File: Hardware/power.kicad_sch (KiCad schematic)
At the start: 31 parts, among them U10 RT9080-3.3, U5 LM66200, U6 AP63357DV-7, U7 LM66200, U8 MAX17048, U9 MCP73831

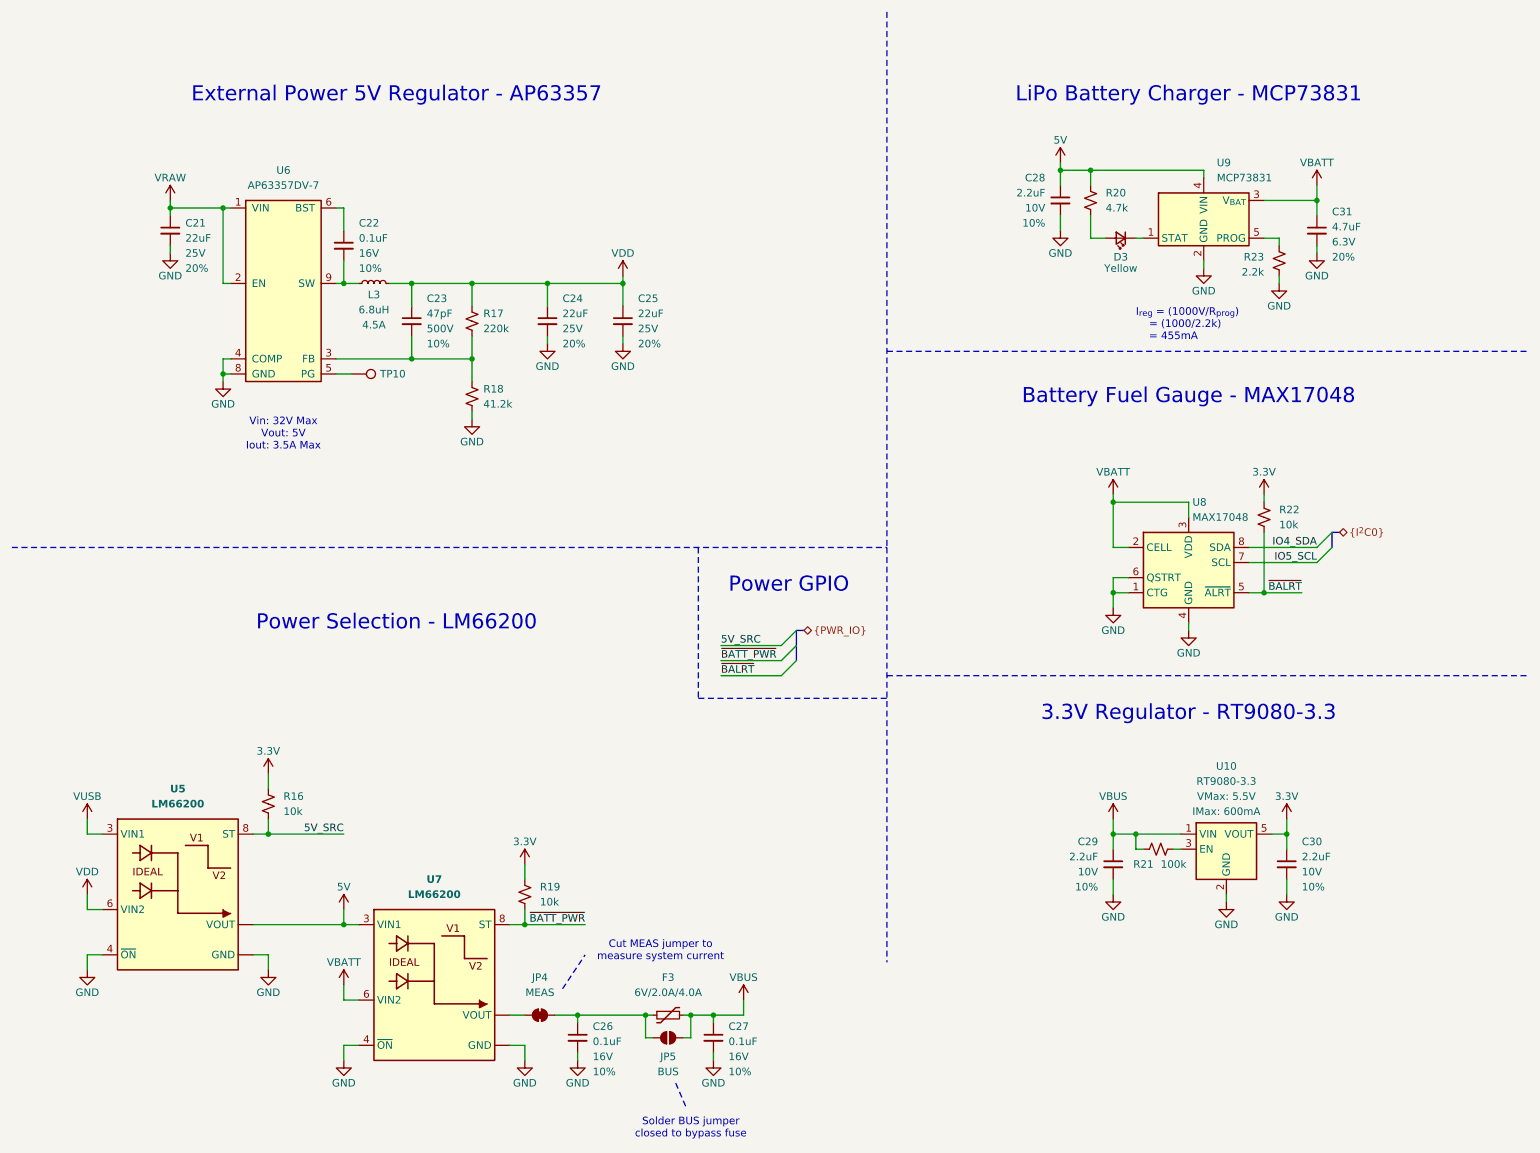
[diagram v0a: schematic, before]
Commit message: Update v01 from checklist. Added measures.
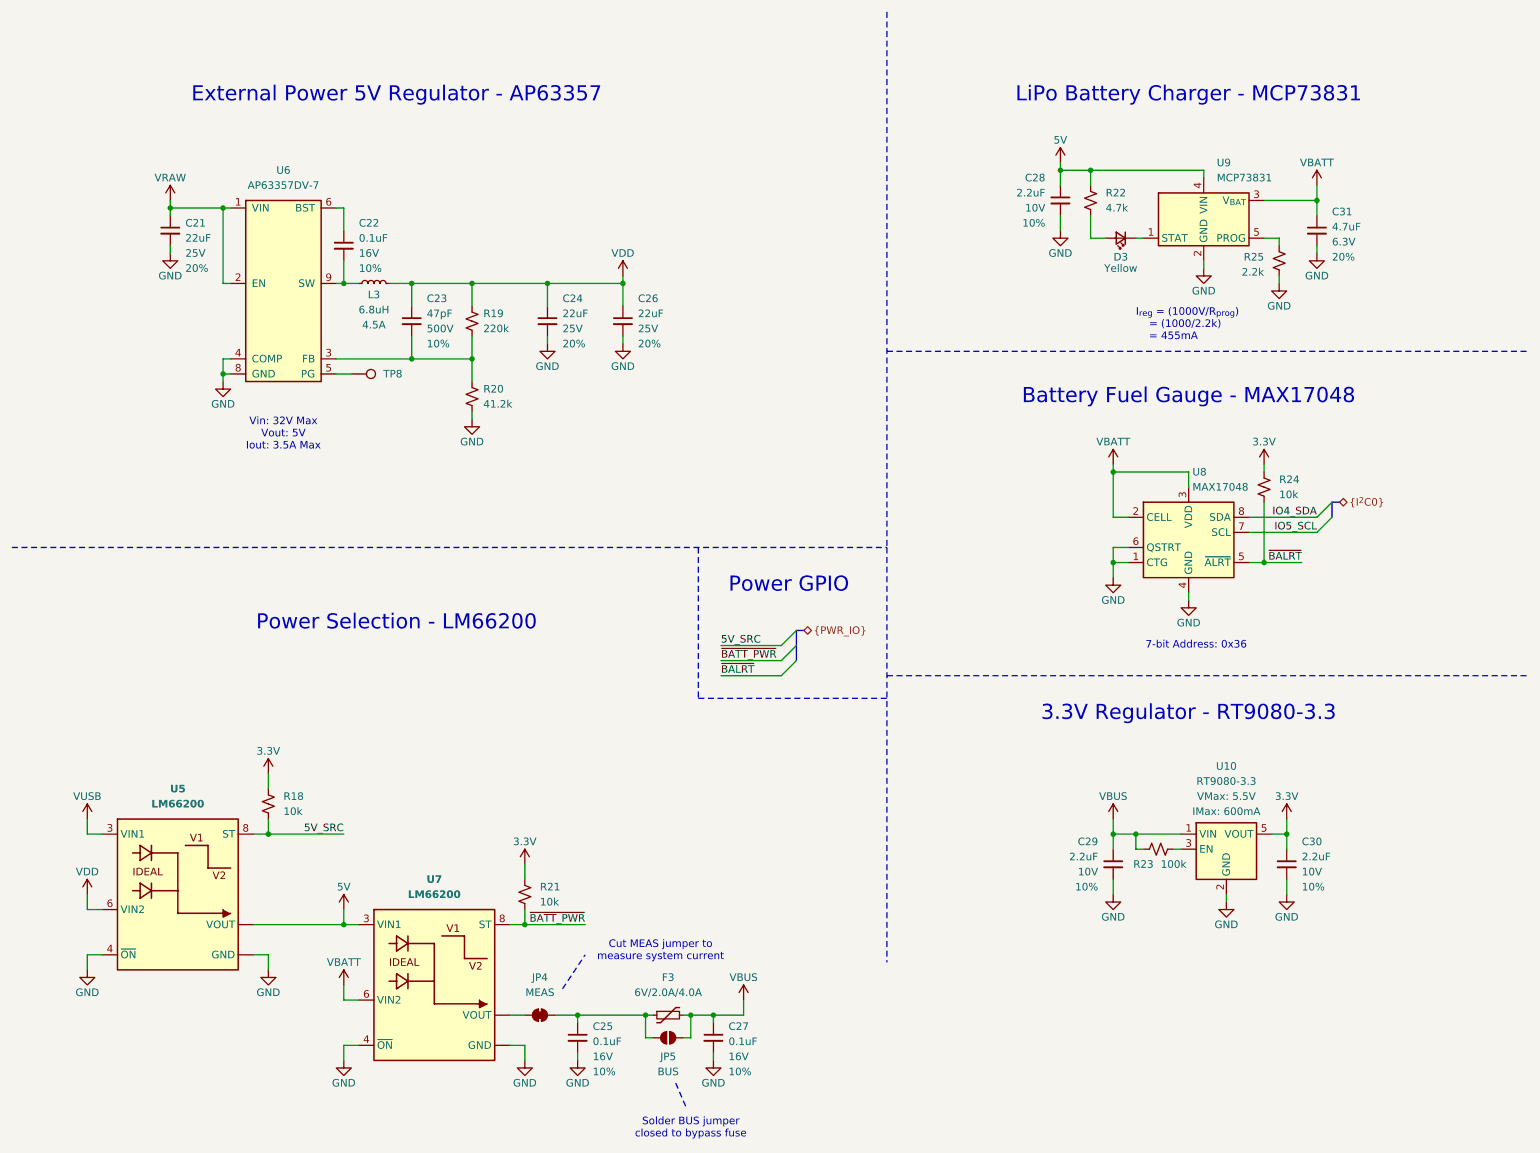
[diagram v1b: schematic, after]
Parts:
- renumbered C26 to C25, C25 to C26, R16 to R18, R17 to R19, R18 to R20, R19 to R21, R20 to R22, R21 to R23, R22 to R24, R23 to R25, TP10 to TP8
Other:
- note added: "7-bit Address: 0x36"
- moved on the sheet: R24, U8

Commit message: v01 post design review changes. Panelize/CAM.
Remove F3.
Added switched power for qwiic, rgb, sd.
Update USB diode for prod friendly package.
Added debounce cap on User button.
Swap user and boot buttons.
Make F2 a smaller package.
Renumber GPIO and use contiguous numbers for PIO purposes.
Swap inputs on Ideal diodes for battery powered current purposes.
Move USB termination resistors closer to MCU.
Fixed A0-A5 ordering.
Update silks.
Add mask to middle of SMD GPIOs.
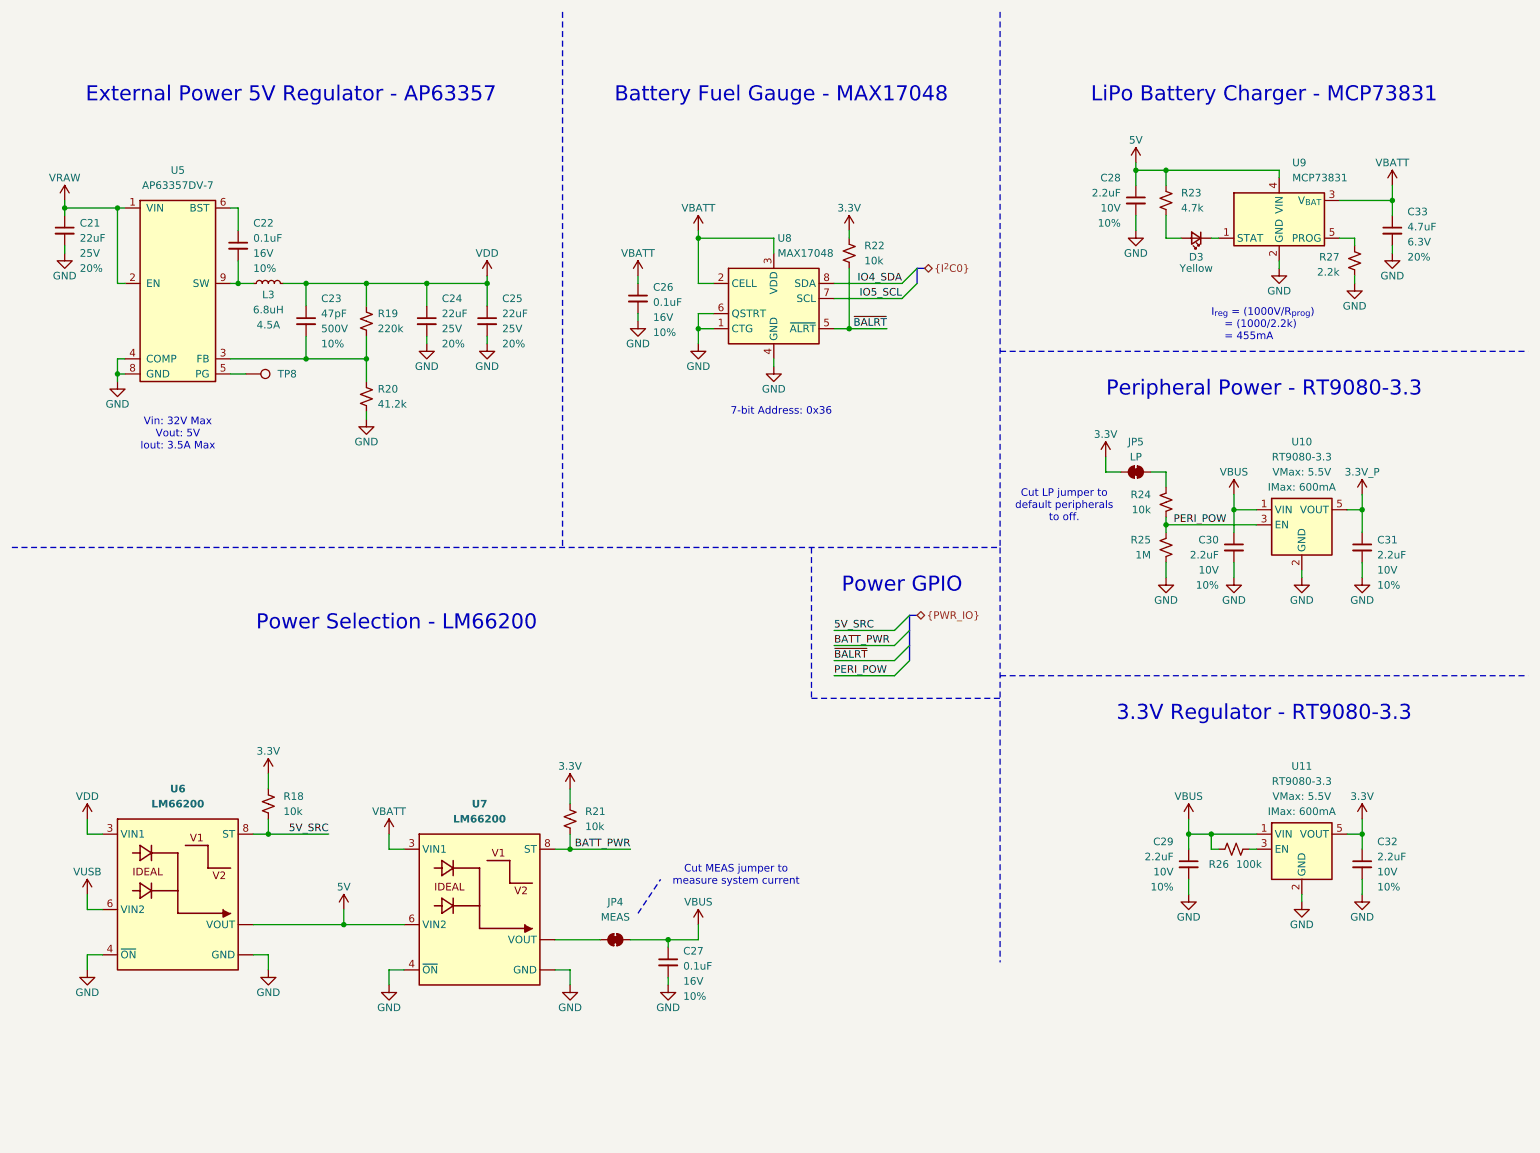
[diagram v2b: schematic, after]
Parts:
- removed C25: 0.1uF, SparkFun-Capacitor:C_0402_1005Metric, symbol SparkFun-Capacitor:0.1uF_0402_16V_10%
- removed F3: 6V/2.0A/4.0A, SparkFun-Fuse:1210, symbol SparkFun-Fuse:Fuse 6V/2.0A/4.0A
- removed JP5: BUS, SparkFun-Jumper:Jumper_2_NO, symbol SparkFun-Jumper:SolderJumper_2_Open
- added C26: 0.1uF, SparkFun-Capacitor:C_0402_1005Metric, symbol SparkFun-Capacitor:0.1uF_0402_16V_10%
- added C30, C31: 2.2uF, SparkFun-Capacitor:C_0402_1005Metric, symbol SparkFun-Capacitor:2.2uF_0402_10V_10%
- added JP5: LP, SparkFun-Jumper:Jumper_2_NC_Trace, symbol SparkFun-Jumper:SolderJumper_2_Bridged
- added R24: 10k, SparkFun-Resistor:R_0402_1005Metric, symbol SparkFun-Resistor:10k_0402
- added R25: 1M, SparkFun-Resistor:R_0402_1005Metric, symbol SparkFun-Resistor:1M_0402
- added U10: RT9080-3.3, SparkFun-Semiconductor-Standard:SOT23-5, symbol SparkFun-Regulator:RT9080-3.3
- renumbered C26 to C25, C30 to C32, C31 to C33, R24 to R22, R22 to R23, R23 to R26, R25 to R27, U10 to U11, U6 to U5, U5 to U6
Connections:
- net 3.3V: now also JP5.1 (A)
- net 5V: now also U7.6 (VIN2); no longer U7.3 (VIN1)
- net GND: now also C26.2, C30.2, C31.2, R25.1, U10.2 (GND)
- net VBATT: now also U7.3 (VIN1), C26.1; no longer U7.6 (VIN2)
- net VBUS: now also JP4.2 (B), C30.1, U10.1 (VIN)
- net VDD: now also U6.3 (VIN1); no longer U6.6 (VIN2)
- net VUSB: now also U6.6 (VIN2); no longer U6.3 (VIN1)
- net ~{BATT_PWR} renamed BATT_PWR
- new net: JP5.2 (B), R24.1
- new net 3.3V_P: C31.1, U10.5 (VOUT)
- new net PERI_POW: R24.2, R25.2, U10.3 (EN)
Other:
- note added: "Cut LP jumper to default peripherals to off."
- note added: "Peripheral Power - RT9080-3.3"
- note removed: "Solder BUS jumper closed to bypass fuse"
- moved on the sheet: C21, C22, C23, C24, C25, C27, C28, C29, C32, C33, D3, JP4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

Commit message: Update for reds
Change version number to v10.
Make user button number correct.
Rotate HSTX conn 180 degrees electrically.
Add silk for HSTX contact direction.
Increase silk text size where it made sense.
Increase silk label length on PTHs.
Panelize and CAM.
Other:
- title: Power Generation and Battery Management -> Power and Battery Management
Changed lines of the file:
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@@
 	(paper "USLetter")
 	(title_block
-		(title "Power Generation and Battery Management")
-		(date "2024-12-03")
-		(rev "v01")
+		(title "Power and Battery Management")
+		(date "2025-02-05")
+		(rev "v10")
 		(company "SparkFun Electronics")
 		(comment 1 "Designed by: Alex Brudner")
